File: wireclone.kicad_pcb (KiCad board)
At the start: 2 copper layers, 45 parts, among them P1 CONN_01X02, P2 CONN_01X03, P3 CONN_01X03, U1 LME49720, U2 LME49720, U3 LME49600, U4 LME49600, U5 LM7812CT, U6 LM7912CT

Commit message: did most of the layout
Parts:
- removed C13, C16: 10u, Capacitors_Tantalum_SMD:Tantalum_Case-C_EIA-6032-28_Reflow
- removed C14, C15: 100n, Capacitors_SMD:C_0805
- removed R11, R12: 0R, Resistors_SMD:R_0805
- added D3: M7, Diodes_SMD:D_SMA, F.Cu at (71.1, 47.0)
- added D4: M7, Diodes_SMD:D_SMA, F.Cu at (71.1, 54.7)
- added REF**: hole3mm, pcb:hole3mm, F.Cu at (151.8, 31.8)
- added REF**: hole3mm, pcb:hole3mm, F.Cu at (151.8, 69.8)
- added REF**: hole3mm, pcb:hole3mm, F.Cu at (62.2, 31.8)
- added REF**: hole3mm, pcb:hole3mm, F.Cu at (62.2, 69.8)
- C1, C2: footprint Capacitors_SMD:C_1206 -> Capacitors_SMD:C_0805
- C10, C11: value 100n -> 10u; footprint Capacitors_SMD:C_0805 -> Capacitors_SMD:C_1206
- C12, C9: footprint Capacitors_Tantalum_SMD:Tantalum_Case-C_EIA-6032-28_Reflow -> Capacitors_SMD:C_1206
- D1, D2: footprint Diodes_SMD:SMA_Standard -> Diodes_SMD:D_SMA
- P1: value CONN_01X02 -> CONN_01X03; footprint Terminal_Blocks:TerminalBlock_Pheonix_MKDS1.5-2pol -> Terminal_Blocks:TerminalBlock_Pheonix_MKDS1.5-3pol
- P2, P3: footprint Terminal_Blocks:TerminalBlock_Pheonix_MKDS1.5-3pol -> Terminal_Blocks:TerminalBlock_Pheonix_MPT-2.54mm_3pol
- U1, U2: footprint SMD_Packages:SOIC-8-N -> Housings_DIP:DIP-8_W7.62mm_Socket
- moved U4 102.7 mm to (123.3, 59.1)
- moved U3 97.6 mm to (123.3, 42.5)
- moved R9 88.0 mm to (113.8, 43.7), turned to 180 degrees
- moved R7 87.2 mm to (110.2, 43.7), turned to 180 degrees
- moved R1 86.8 mm to (110.2, 29.8)
- moved C20 84.0 mm to (75.9, 31.7), turned to 270 degrees
- moved C12 83.6 mm to (124.5, 52.8)
- moved R2 81.5 mm to (105.7, 47.2), turned to 180 degrees
- moved R5 81.5 mm to (110.2, 47.2), turned to 180 degrees
- moved P3 74.0 mm to (118.1, 83.2)
- moved C4 71.4 mm to (103.5, 29.8)
- moved C22 70.8 mm to (94.9, 47.4), turned to 270 degrees
- moved U1 69.2 mm to (111.8, 33.0), turned to 270 degrees
- moved C10 64.7 mm to (124.5, 36.2)
- moved C21 63.7 mm to (94.9, 54.0), turned to 270 degrees
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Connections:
- C10 pad 2: /PSU/VCC -> /PSU/VEE
- C11 pad 2: /PSU/VEE -> /PSU/VCC
- C9 pad 1: /PSU/VCC -> GND
- C9 pad 2: GND -> /PSU/VCC
- D1 pad 1: Net-(D1-Pad1) -> /PSU/AC2
- D2 pad 2: Net-(D1-Pad1) -> /PSU/AC2
- P1 pad 1: GND -> /PSU/AC2
- P1 pad 2: Net-(D1-Pad1) -> GND
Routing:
- net /PSU/VCC: track 0.00 -> 91.8 mm, vias 0 -> 3
- net /PSU/VEE: track 0.00 -> 88.0 mm, vias 0 -> 7
- net Net-(C18-Pad2): track 0.00 -> 34.1 mm
- net /amplifiers/OUTL: track 0.00 -> 33.2 mm
- net /PSU/AC2: track 0.00 -> 20.1 mm, vias 0 -> 1
- net GND: track 0.00 -> 19.1 mm, vias 0 -> 9
- net Net-(C1-Pad2): track 0.00 -> 18.0 mm
- net Net-(R1-Pad1): track 0.00 -> 16.5 mm
- net /amplifiers/INL: track 0.00 -> 15.0 mm
- net /PSU/AC1: track 0.00 -> 14.4 mm
- net Net-(C7-Pad2): track 0.00 -> 7.88 mm
- net Net-(C7-Pad1): track 0.00 -> 6.50 mm
- net Net-(U1-Pad1): track 0.00 -> 1.05 mm
- added copper zone on B.Cu, net /PSU/VEE
- added copper zone on F.Cu, net /PSU/VEE
- added copper zone on B.Cu, net GND
- added copper zone on F.Cu, net Net-(C17-Pad1)
- added copper zone on F.Cu, net Net-(C18-Pad2)
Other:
- board outline added: 99.7 x 48.3 mm
- net class PWR added: clearance 0.25, trace_width 1, via_dia 0.6, via_drill 0.4

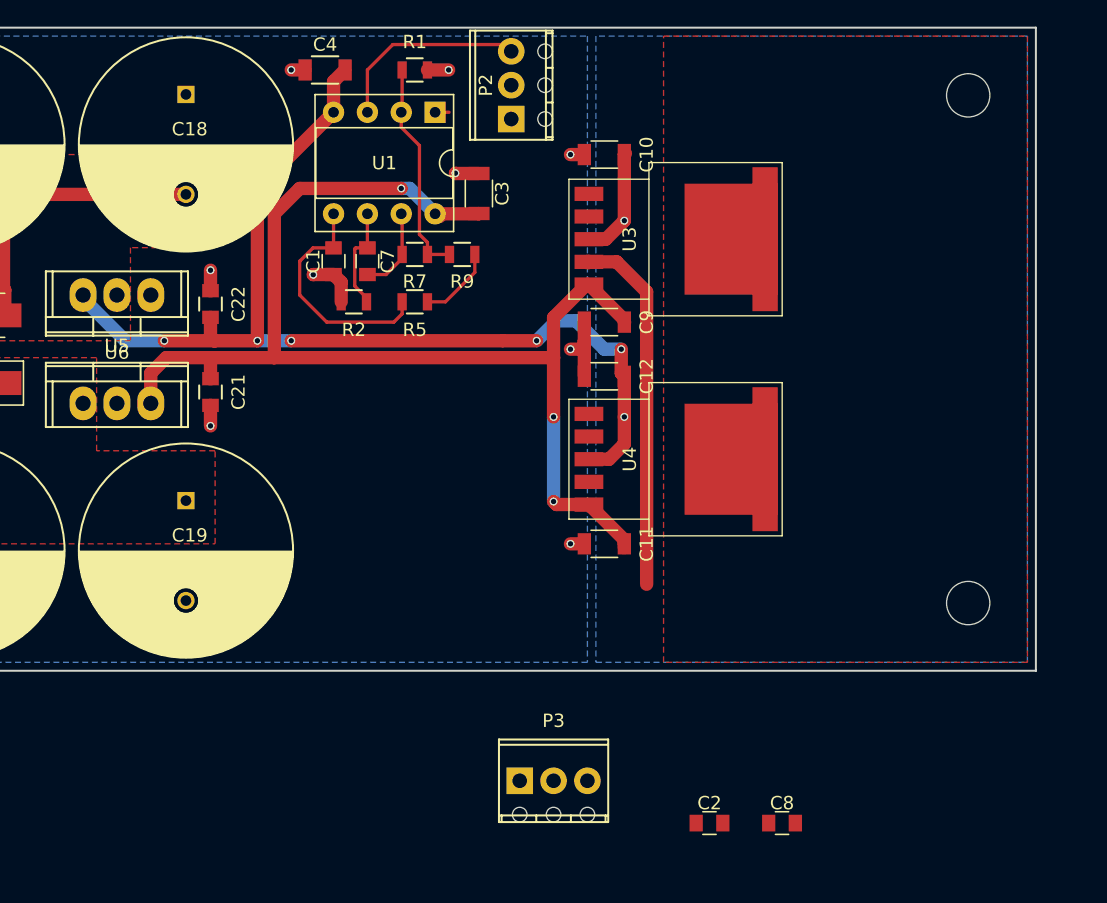
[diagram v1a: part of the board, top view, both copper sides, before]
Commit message: moved output to end, stitched thermal plane
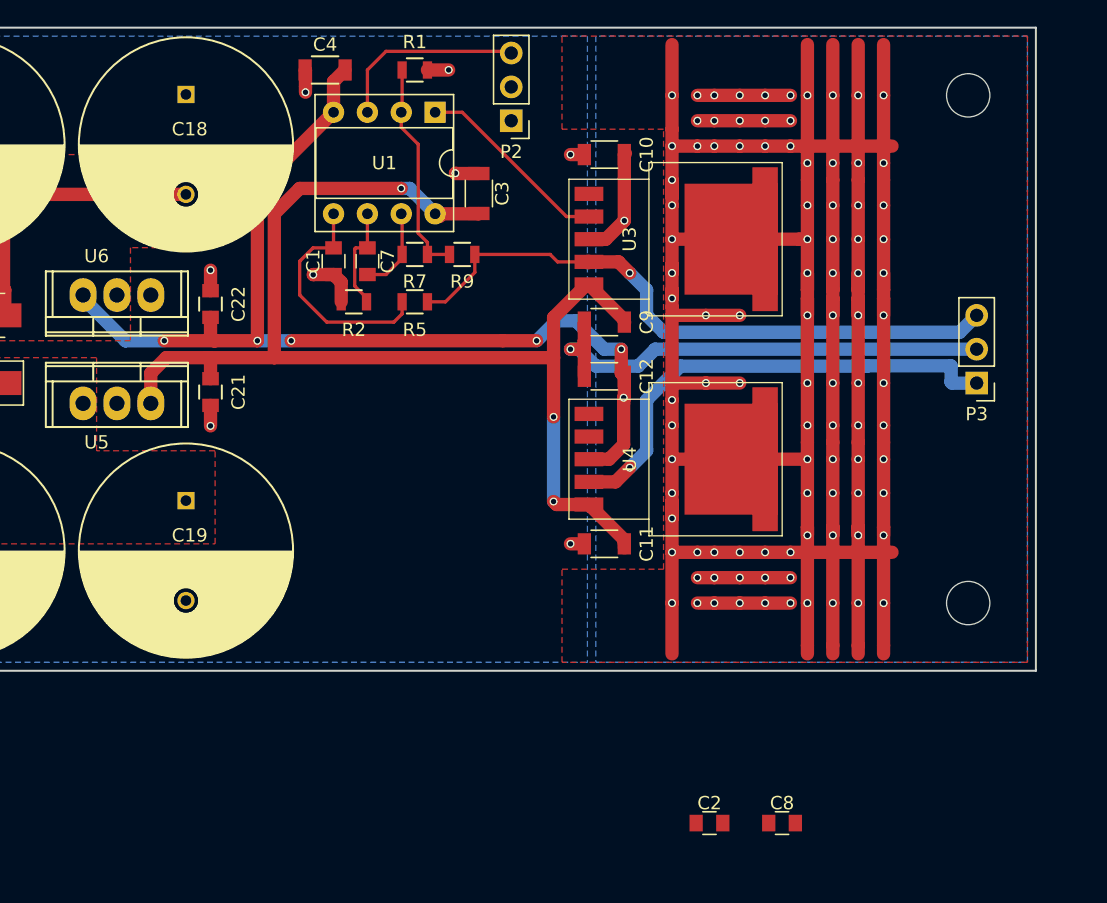
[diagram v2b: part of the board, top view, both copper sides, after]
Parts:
- P2, P3: footprint Terminal_Blocks:TerminalBlock_Pheonix_MPT-2.54mm_3pol -> Pin_Headers:Pin_Header_Straight_1x03_Pitch2.54mm
- moved P3 45.5 mm to (152.4, 53.3), turned to 180 degrees
- moved P2 0.13 mm to (117.5, 33.7), turned to 180 degrees
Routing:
- net /PSU/VEE: track 88.0 -> 424.6 mm, vias 7 -> 103
- net /amplifiers/OUTR: track 0.00 -> 36.2 mm, vias 0 -> 1
- net GND: track 19.1 -> 51.3 mm
- net /amplifiers/OUTL: track 33.2 -> 47.8 mm, vias 0 -> 1
- net Net-(U1-Pad1): track 1.05 -> 14.8 mm

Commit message: complete layout drafted
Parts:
- added P4: CONN_01X02, Pin_Headers:Pin_Header_Straight_1x02_Pitch2.54mm, F.Cu at (118.7, 72.4)
- P2: value CONN_01X03 -> CONN_01X02; footprint Pin_Headers:Pin_Header_Straight_1x03_Pitch2.54mm -> Pin_Headers:Pin_Header_Straight_1x02_Pitch2.54mm
- moved R10 78.3 mm to (113.8, 67.9), turned to 180 degrees
- moved R8 77.4 mm to (110.2, 67.9), turned to 180 degrees
- moved R3 74.0 mm to (110.2, 53.8)
- moved C6 73.7 mm to (103.1, 53.8)
- moved R4 72.0 mm to (105.4, 71.8), turned to 180 degrees
- moved R6 71.7 mm to (110.2, 71.8), turned to 180 degrees
- moved U2 56.7 mm to (111.8, 57.1), turned to 270 degrees
- moved C5 56.2 mm to (115.6, 63.3), turned to 270 degrees
- moved C8 35.8 mm to (106.7, 68.6), turned to 90 degrees
- moved C2 33.3 mm to (104.1, 68.6), turned to 90 degrees
- moved P2 5.24 mm to (118.7, 28.6), turned to 0 degrees
- moved C18 1.27 mm to (91.8, 31.7)
- moved C19 1.27 mm to (91.8, 62.2)
- moved C17 1.27 mm to (74.6, 62.2)
- moved C20 1.27 mm to (74.6, 31.7)
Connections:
- P2 pad 1: /amplifiers/INR -> /amplifiers/INL
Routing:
- net /amplifiers/INR: track 0.00 -> 36.1 mm, vias 0 -> 2
- net /PSU/VEE: track 424.6 -> 459.3 mm, vias 103 -> 94
- net /PSU/VCC: track 91.8 -> 117.9 mm, vias 3 -> 4
- net /amplifiers/OUTR: track 36.2 -> 56.0 mm
- net Net-(C2-Pad2): track 0.00 -> 17.1 mm
- net Net-(R10-Pad2): track 0.00 -> 16.6 mm
- net Net-(U2-Pad1): track 0.00 -> 11.6 mm
- net Net-(C8-Pad2): track 0.00 -> 8.77 mm
- net GND: track 51.3 -> 59.7 mm, vias 9 -> 13
- net Net-(C8-Pad1): track 0.00 -> 6.66 mm
- net /amplifiers/INL: track 14.5 -> 16.3 mm

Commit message: Beautification
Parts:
- added REF***: OSHW-Logo2_7.3x6mm_SilkScreen, Symbols:OSHW-Logo2_7.3x6mm_SilkScreen, F.Cu at (152.4, 41.1)
- moved P2 0.90 mm to (119.4, 29.2)
- moved P4 0.63 mm to (119.4, 72.4)
- moved C5 0.51 mm to (115.1, 63.3)
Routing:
- net /amplifiers/INL: track 16.3 -> 17.8 mm
- net /amplifiers/INR: track 36.1 -> 35.0 mm
- net /PSU/VCC: track 117.9 -> 117.4 mm
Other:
- outline, holes or cut-outs redrawn
- board text added: "Headphone Amplifier"
- board text added: "L In"
- board text added: "LME49600 Appnote Amplifier"
- board text added: "Out"
- board text added: "R In"
- board text added: "Rev.A 201710"
- board text added: "github.com/phenidone"
- board text added: "william@brodie-tyrrell.org"
- board text added: "~~12"
- board text added: "~~12V"

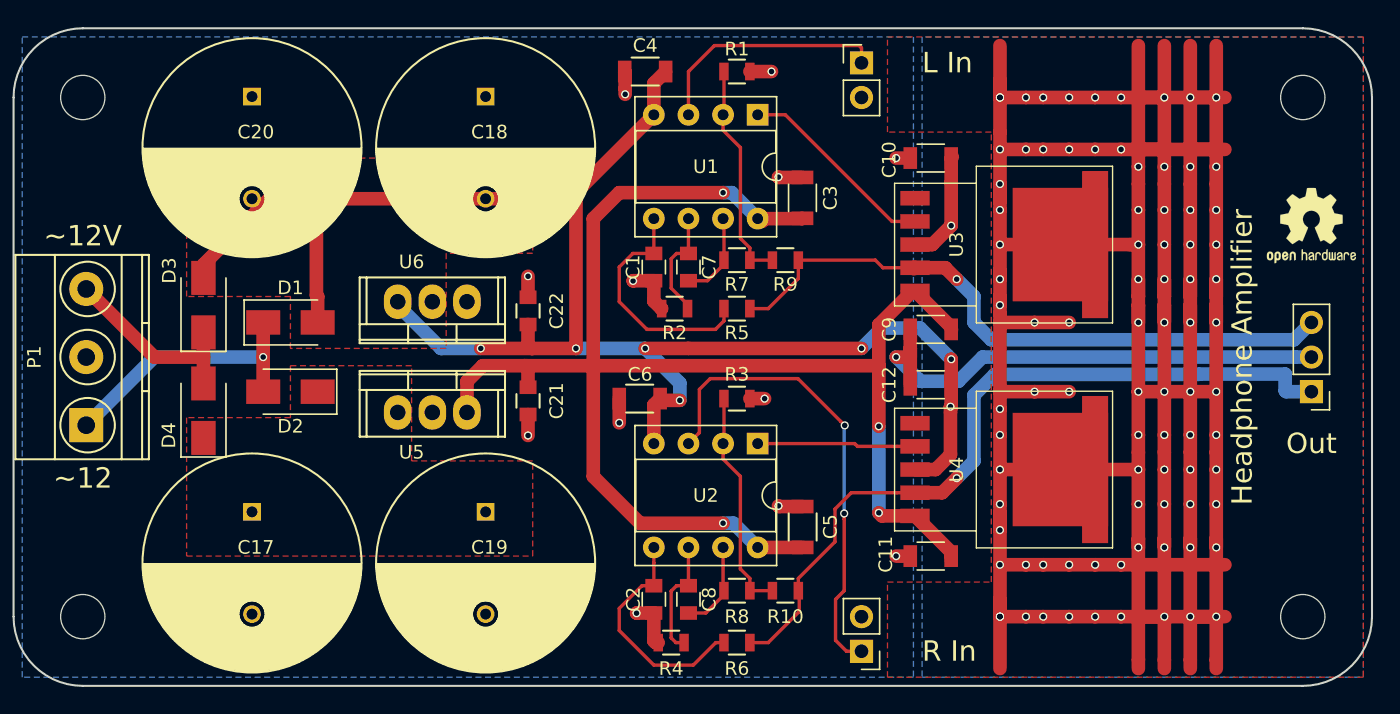
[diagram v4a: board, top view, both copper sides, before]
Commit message: shortened board
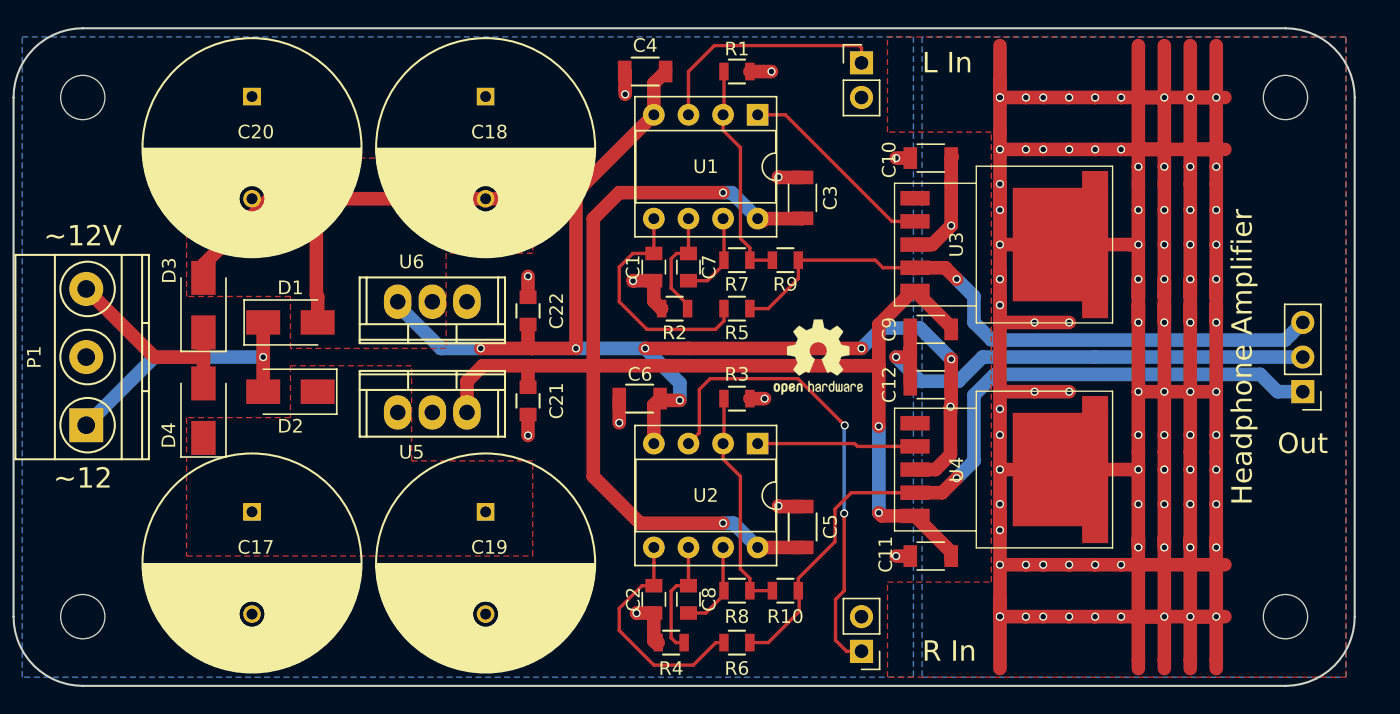
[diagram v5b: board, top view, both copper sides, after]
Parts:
- moved REF*** 37.5 mm to (116.2, 50.8)
- moved REF** 1.27 mm to (150.5, 31.8)
- moved REF** 1.27 mm to (150.5, 69.8)
- moved P3 0.64 mm to (151.8, 53.3)
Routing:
- net /amplifiers/OUTR: track 56.3 -> 55.0 mm
- net GND: track 60.1 -> 59.4 mm
- net /amplifiers/OUTL: track 47.8 -> 47.1 mm
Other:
- board size 99.7 x 48.3 mm -> 98.4 x 48.3 mm
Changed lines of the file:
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@@
     (thickness 1.6)
     (drawings 18)
-    (tracks 519)
+    (tracks 520)
     (zones 0)
     (modules 47)
@@
   )
   (module Pin_Headers:Pin_Header_Straight_1x03_Pitch2.54mm (layer F.Cu)
-    (at 152.4 53.34 180)
+    (at 151.765 53.34 180)
     (descr "Through hole straight pin header, 1x03, 2.54mm pitch, single row")
     (tags "Through hole pin header THT 1x03 2.54mm single row")
@@
   )
   (module pcb:hole3mm (layer F.Cu)
-    (at 151.765 31.75)
+    (at 150.495 31.75)
     (fp_text reference REF** (at 0 0.5) (layer F.SilkS) hide
       (effects (font (size 1 1) (thickness 0.15)))
@@
   )
   (module pcb:hole3mm (layer F.Cu)
-    (at 151.765 69.85)
+    (at 150.495 69.85)
     (fp_text reference REF** (at 0 0.5) (layer F.SilkS) hide
       (effects (font (size 1 1) (thickness 0.15)))
@@
   )
   (module Symbols:OSHW-Logo2_7.3x6mm_SilkScreen (layer F.Cu)
-    (at 152.4 41.148)
+    (at 116.205 50.8)
     (descr "Open Source Hardware Symbol")
     (tags "Logo Symbol OSHW")
@@
     (effects (font (size 1.5 1.5) (thickness 0.3)) (justify mirror))
   )
-  (gr_text Out (at 152.4 57.15) (layer F.SilkS)
+  (gr_text Out (at 151.765 57.15) (layer F.SilkS)
     (effects (font (size 1.5 1.5) (thickness 0.3)))
   )
   (gr_arc (start 62.23 31.75) (end 57.15 31.75) (angle 90) (layer Edge.Cuts) (width 0.15))
   (gr_arc (start 62.23 69.85) (end 62.23 74.93) (angle 90) (layer Edge.Cuts) (width 0.15))
-  (gr_arc (start 151.765 69.85) (end 156.845 69.85) (angle 90) (layer Edge.Cuts) (width 0.15))
-  (gr_arc (start 151.765 31.75) (end 151.765 26.67) (angle 90) (layer Edge.Cuts) (width 0.15))
+  (gr_arc (start 150.495 69.85) (end 155.575 69.85) (angle 90) (layer Edge.Cuts) (width 0.15))
+  (gr_arc (start 150.495 31.75) (end 150.495 26.67) (angle 90) (layer Edge.Cuts) (width 0.15))
   (gr_text "R In" (at 123.825 72.39) (layer F.SilkS)
     (effects (font (size 1.5 1.5) (thickness 0.3)) (justify left))
@@
     (effects (font (size 1.5 1.5) (thickness 0.3)))
   )
-  (gr_line (start 151.765 26.67) (end 62.23 26.67) (layer Edge.Cuts) (width 0.15))
-  (gr_line (start 156.845 69.85) (end 156.845 31.75) (layer Edge.Cuts) (width 0.15))
-  (gr_line (start 62.23 74.93) (end 151.765 74.93) (layer Edge.Cuts) (width 0.15))
+  (gr_line (start 150.495 26.67) (end 62.23 26.67) (layer Edge.Cuts) (width 0.15))
+  (gr_line (start 155.575 69.85) (end 155.575 31.75) (layer Edge.Cuts) (width 0.15))
+  (gr_line (start 62.23 74.93) (end 150.495 74.93) (layer Edge.Cuts) (width 0.15))
   (gr_line (start 57.15 31.75) (end 57.15 69.85) (layer Edge.Cuts) (width 0.15))
+  (segment (start 128.27 50.8) (end 136.525 50.8) (width 1) (layer B.Cu) (net 1))
+  (segment (start 136.525 50.8) (end 151.765 50.8) (width 1) (layer B.Cu) (net 1))
   (segment (start 121.92 50.8) (end 123.69377 52.57377) (width 1) (layer B.Cu) (net 1))
-  (segment (start 128.27 50.8) (end 151.197919 50.8) (width 1) (layer B.Cu) (net 1))
   (segment (start 123.69377 52.57377) (end 126.49623 52.57377) (width 1) (layer B.Cu) (net 1))
   (segment (start 126.49623 52.57377) (end 128.27 50.8) (width 1) (layer B.Cu) (net 1))
-  (segment (start 151.197919 50.8) (end 152.4 50.8) (width 1) (layer B.Cu) (net 1))
   (segment (start 111.186 53.848) (end 112.268 53.848) (width 1) (layer F.Cu) (net 1))
   (via (at 112.268 53.848) (size 0.6) (drill 0.4) (layers F.Cu B.Cu) (net 1))
@@
   (segment (start 117.475 71.585) (end 117.475 68.58) (width 0.25) (layer F.Cu) (net 13))
   (segment (start 119.38 72.39) (end 118.28 72.39) (width 0.25) (layer F.Cu) (net 13))
+  (segment (start 128.905 49.53) (end 129.794 49.53) (width 1) (layer B.Cu) (net 14))
+  (segment (start 150.47501 49.54999) (end 150.915001 49.109999) (width 1) (layer B.Cu) (net 14))
+  (segment (start 129.794 49.53) (end 129.81399 49.54999) (width 1) (layer B.Cu) (net 14))
+  (segment (start 129.81399 49.54999) (end 150.47501 49.54999) (width 1) (layer B.Cu) (net 14))
+  (segment (start 150.915001 49.109999) (end 151.765 48.26) (width 1) (layer B.Cu) (net 14))
   (segment (start 126.365 45.085) (end 127.635 46.355) (width 1) (layer B.Cu) (net 14))
   (segment (start 127.635 46.355) (end 127.635 48.26) (width 1) (layer B.Cu) (net 14))
   (segment (start 127.635 48.26) (end 128.905 49.53) (width 1) (layer B.Cu) (net 14))
-  (segment (start 128.905 49.53) (end 151.13 49.53) (width 1) (layer B.Cu) (net 14))
-  (segment (start 151.13 49.53) (end 152.4 48.26) (width 1) (layer B.Cu) (net 14))
   (segment (start 123.305 44.245) (end 125.525 44.245) (width 1) (layer F.Cu) (net 14))
   (segment (start 125.525 44.245) (end 126.365 45.085) (width 1) (layer F.Cu) (net 14))
@@
   (segment (start 112.536 47.244) (end 114.742 45.038) (width 0.25) (layer F.Cu) (net 14))
   (segment (start 114.742 45.038) (end 114.742 43.688) (width 0.25) (layer F.Cu) (net 14))
+  (segment (start 126.365 59.69) (end 127.635 58.42) (width 1) (layer B.Cu) (net 15))
+  (segment (start 127.635 58.42) (end 127.635 53.590919) (width 1) (layer B.Cu) (net 15))
+  (segment (start 127.635 53.590919) (end 129.155919 52.07) (width 1) (layer B.Cu) (net 15))
+  (segment (start 129.155919 52.07) (end 148.645 52.07) (width 1) (layer B.Cu) (net 15))
+  (segment (start 148.645 52.07) (end 149.915 53.34) (width 1) (layer B.Cu) (net 15))
+  (segment (start 149.915 53.34) (end 151.765 53.34) (width 1) (layer B.Cu) (net 15))
   (segment (start 121.975 60.755) (end 123.305 60.755) (width 0.25) (layer F.Cu) (net 15))
   (segment (start 118.633948 60.755) (end 121.975 60.755) (width 0.25) (layer F.Cu) (net 15))
@@
   (segment (start 117.433587 64.353413) (end 117.433587 61.955361) (width 0.25) (layer F.Cu) (net 15))
   (segment (start 114.742 67.945) (end 114.742 67.045) (width 0.25) (layer F.Cu) (net 15))
-  (segment (start 144.145 52.07) (end 129.155919 52.07) (width 1) (layer B.Cu) (net 15))
-  (segment (start 129.155919 52.07) (end 127.635 53.590919) (width 1) (layer B.Cu) (net 15))
-  (segment (start 127.635 53.590919) (end 127.635 58.42) (width 1) (layer B.Cu) (net 15))
-  (segment (start 127.635 58.42) (end 126.365 59.69) (width 1) (layer B.Cu) (net 15))
   (segment (start 114.808 68.311) (end 114.808 69.483) (width 0.25) (layer F.Cu) (net 15))
   (segment (start 114.808 69.483) (end 112.536 71.755) (width 0.25) (layer F.Cu) (net 15))
@@
   (segment (start 114.742 67.945) (end 114.742 68.245) (width 0.25) (layer F.Cu) (net 15))
   (segment (start 114.742 68.245) (end 114.808 68.311) (width 0.25) (layer F.Cu) (net 15))
-  (segment (start 150.47501 52.05001) (end 150.47501 53.26501) (width 1) (layer B.Cu) (net 15))
-  (segment (start 150.47501 53.26501) (end 150.55 53.34) (width 1) (layer B.Cu) (net 15))
-  (segment (start 150.55 53.34) (end 152.4 53.34) (width 1) (layer B.Cu) (net 15))
-  (segment (start 150.47501 52.05001) (end 144.16499 52.05001) (width 1) (layer B.Cu) (net 15))
   (segment (start 123.305 60.755) (end 125.3 60.755) (width 1) (layer F.Cu) (net 15))
   (segment (start 125.3 60.755) (end 126.365 59.69) (width 1) (layer F.Cu) (net 15))
@@
     (polygon
       (pts
-        (xy 156.21 27.305) (xy 156.21 74.295) (xy 121.285 74.295) (xy 121.285 67.31) (xy 128.905 67.31)
+        (xy 154.94 27.305) (xy 154.94 74.295) (xy 121.285 74.295) (xy 121.285 67.31) (xy 128.905 67.31)
         (xy 128.905 34.29) (xy 121.285 34.29) (xy 121.285 27.305)
       )
@@
     (polygon
       (pts
-        (xy 156.21 27.305) (xy 123.825 27.305) (xy 123.825 74.295) (xy 156.21 74.295)
+        (xy 154.94 27.305) (xy 123.825 27.305) (xy 123.825 74.295) (xy 154.94 74.295)
       )
     )
